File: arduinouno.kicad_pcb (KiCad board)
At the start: 2 copper layers, 0 parts

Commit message: started placement; updated 3d model offsets for PDIP components
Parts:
- added C1: 100u|10V, arduinouno:C_ALUM_C_SIZE, F.Cu at (212.8, 44.3)
- added C10: 18pF, arduinouno:C0805x95mm, F.Cu at (201.9, 71.8)
- added C11: 100nF, arduinouno:C0805x95mm, F.Cu at (214.3, 52.2)
- added C12: 10uF|16V, arduinouno:C0805x145mm, F.Cu at (210.6, 56.0)
- added C13: 10uF|16V, arduinouno:C0805x145mm, F.Cu at (191.9, 75.0)
- added C14: 100nF, arduinouno:C0805x95mm, F.Cu at (195.2, 71.1)
- added C15: 100nF, arduinouno:C0805x95mm, F.Cu at (203.6, 63.6)
- added C16: 100nF, arduinouno:C0805x95mm, F.Cu at (195.2, 69.0)
- added C17: 100nF, arduinouno:C0805x95mm, F.Cu at (191.9, 73.0)
- added C19: 10uF|16V, arduinouno:C0805x145mm, F.Cu at (148.9, 96.2)
- added C2: 100uF|10V, arduinouno:C_ALUM_C_SIZE, F.Cu at (205.4, 55.6)
- added C20: 100nF, arduinouno:C0805x95mm, F.Cu at (147.2, 81.4)
- added C21: 10uF|16V, arduinouno:C0805x145mm, F.Cu at (206.5, 59.5)
- added C22: 10uF|16V, arduinouno:C0805x145mm, F.Cu at (143.4, 96.2)
- added C23: 100nF, arduinouno:C0805x95mm, F.Cu at (143.4, 94.1)
- added C24: 100nF, arduinouno:C0805x95mm, F.Cu at (146.8, 94.1)
- added C25: 18pF, arduinouno:C0805x95mm, F.Cu at (143.8, 79.3)
- added C26: 100nF, arduinouno:C0805x95mm, F.Cu at (200.3, 63.7)
- added C27: 18pF, arduinouno:C0805x95mm, F.Cu at (147.2, 79.3)
- added C28: 100nF, arduinouno:C0805x95mm, F.Cu at (188.5, 76.8)
- added C29: 100nF, arduinouno:C0805x95mm, F.Cu at (210.9, 51.9)
- added C3: 10uF|16V, arduinouno:C0805x145mm, F.Cu at (191.9, 70.9)
- added C30: 100nF, arduinouno:C0805x95mm, F.Cu at (200.3, 61.6)
- added C31: 100nF, arduinouno:C0805x95mm, F.Cu at (210.3, 65.6)
- added C32: 100nF, arduinouno:C0805x95mm, F.Cu at (198.6, 77.2)
- added C33: 100nF, arduinouno:C0805x95mm, F.Cu at (198.4, 67.0)
- added C34: 10uF|16V, arduinouno:C0805x145mm, F.Cu at (198.0, 89.1)
- added C4: 100nF, arduinouno:C0805x95mm, F.Cu at (214.3, 48.1)
- added C5: 100nF, arduinouno:C0805x95mm, F.Cu at (213.7, 60.4)
- added C6: 100nF, arduinouno:C0805x95mm, F.Cu at (201.9, 73.8)
- added C7: 1uF|25V, arduinouno:C0805x95mm, F.Cu at (205.3, 69.7)
- added C8: 100nF, arduinouno:C0805x95mm, F.Cu at (194.6, 79.3)
- added C9: 18pF, arduinouno:C0805x95mm, F.Cu at (205.3, 67.7)
- added D1: GREEN, arduinouno:LED_0603, F.Cu at (197.4, 97.8)
- added D2: ORANGE, arduinouno:LED_0603, F.Cu at (214.8, 84.4)
- added D3: ORANGE, arduinouno:LED_0603, F.Cu at (200.9, 97.8)
- added D4: ORANGE, arduinouno:LED_0603, F.Cu at (197.4, 99.4)
- added D5: BAT54HT1G, arduinouno:SOD323, F.Cu at (194.6, 88.8)
- added D6: BAT54HT1G, arduinouno:SOD323, F.Cu at (181.8, 99.0)
- added FB1: MPZ2012S601AT000, arduinouno:FB0805x85mm, F.Cu at (216.4, 97.7)
- added FB2: MPZ2012S601AT000, arduinouno:FB0805x85mm, F.Cu at (148.9, 98.3)
- added FB3: MPZ2012S601AT000, arduinouno:FB0805x85mm, F.Cu at (146.2, 96.8)
- added FID1: FID_1MM, arduinouno:FID_40x120M, F.Cu at (192.1, 90.1)
- added FID2: FID_1MM, arduinouno:FID_40x120M, F.Cu at (191.1, 90.1)
- added FID3: FID_1MM, arduinouno:FID_40x120M, F.Cu at (181.2, 100.3)
- added FID4: FID_1MM, arduinouno:FID_40x120M, F.Cu at (180.2, 100.3)
- added J1: M20-7820842, arduinouno:8P_Header_Female_2.54mm, F.Cu at (129.5, 101.6)
- added J2: M20-7820646, arduinouno:6P_Header_Female_2.54mm, F.Cu at (152.4, 101.6)
- added J3: M20-7820842, arduinouno:8P_Header_Female_2.54mm, F.Cu at (165.1, 53.3)
- added J4: M20-7821046, arduinouno:10P_Header_Female_2.54mm, F.Cu at (143.3, 53.3)
- added J5: 67997-106HLF, arduinouno:HDR_2x3_2.54mm, F.Cu at (195.4, 51.8)
- added J6: 67997-106HLF, arduinouno:HDR_2x3_2.54mm, F.Cu at (211.5, 94.5)
- added J7: 10118193-0001LF, arduinouno:10118193, F.Cu at (185.3, 93.7)
- added J8: PAD_WITH_HOLE_4mmx1.5mm, arduinouno:PAD_WITH_HOLE_4mmx1.5mm, F.Cu at (208.7, 97.9)
- added J9: PAD_WITH_HOLE_4mmx1.5mm, arduinouno:PAD_WITH_HOLE_4mmx1.5mm, F.Cu at (212.7, 97.9)
- added JP1: 68000-103HLF, arduinouno:3P_Header_2.54mm, F.Cu at (205.3, 92.0)
- added JP2: 68602-104HLF, arduinouno:HDR_2x2_2.54mm, F.Cu at (194.7, 64.6)
- added JP3: 68001-204HLF, arduinouno:4P_Header_2.54mm, F.Cu at (211.6, 81.6)
- added JP4: 68000-103HLF, arduinouno:3P_Header_2.54mm, F.Cu at (192.7, 49.2)
- added L1: 2u2|2A, arduinouno:C1210_INDUCTOR, F.Cu at (215.9, 81.9)
- added MH1: MH_7.4MMCx3.2MMD, arduinouno:MH_7.4MMCx3.2MMD, F.Cu at (115.6, 101.6)
- added MH2: MH_7.4MMCx3.2MMD, arduinouno:MH_7.4MMCx3.2MMD, F.Cu at (167.6, 96.5)
- added MH3: MH_7.4MMCx3.2MMD, arduinouno:MH_7.4MMCx3.2MMD, F.Cu at (167.6, 68.6)
- added MH4: MH_7.4MMNCx3.2MMD, arduinouno:MH_7.4MMCx3.2MMD_NON_COPPER_NPTH, F.Cu at (116.8, 53.3)
- added R1: 100K, arduinouno:R0805x60mm, F.Cu at (217.6, 48.3)
- added R10: 1k, arduinouno:R0805x60mm, F.Cu at (207.0, 61.5)
- added R11: 1k, arduinouno:R0805x60mm, F.Cu at (207.0, 63.6)
- added R12: 1k, arduinouno:R0805x60mm, F.Cu at (195.2, 75.2)
- added R13: 22R, arduinouno:R0805x60mm, F.Cu at (139.9, 94.1)
- added R14: 10k, arduinouno:R0805x60mm, F.Cu at (162.7, 81.4)
- added R15: 560R, arduinouno:R0805x60mm, F.Cu at (198.6, 71.1)
- added R16: 1M, arduinouno:R0805x60mm, F.Cu at (143.8, 81.4)
- added R17: 560R, arduinouno:R0805x60mm, F.Cu at (201.9, 67.7)
- added R18: 10k, arduinouno:R0805x60mm, F.Cu at (213.2, 58.4)
- added R19: 10k, arduinouno:R0805x60mm, F.Cu at (201.9, 69.7)
- added R2: 560R, arduinouno:R0805x60mm, F.Cu at (187.9, 79.8)
- added R20: 10k, arduinouno:R0805x60mm, F.Cu at (191.3, 81.2)
- added R21: 10k, arduinouno:R0805x60mm, F.Cu at (198.6, 73.1)
- added R22: 560R, arduinouno:R0805x60mm, F.Cu at (217.3, 54.5)
- added R23: 22R, arduinouno:R0805x60mm, F.Cu at (195.2, 77.2)
- added R24: 22R, arduinouno:R0805x60mm, F.Cu at (207.0, 65.6)
- added R25: 22R, arduinouno:R0805x60mm, F.Cu at (210.3, 61.5)
- added R26: 0R, arduinouno:R0805x60mm, F.Cu at (210.3, 63.6)
- added R27: 0R, arduinouno:R0805x60mm, F.Cu at (217.3, 56.5)
- added R28: 0R, arduinouno:R0805x60mm, F.Cu at (198.6, 75.2)
- added R3: 560R, arduinouno:R0805x60mm, F.Cu at (198.6, 69.0)
- added R4: 10k, arduinouno:R0805x60mm, F.Cu at (217.6, 50.4)
- added R5: 22R, arduinouno:R0805x60mm, F.Cu at (209.9, 59.5)
- added R6: 22R, arduinouno:R0805x60mm, F.Cu at (214.0, 54.3)
- added R7: 22R, arduinouno:R0805x60mm, F.Cu at (191.9, 77.1)
- added R8: 0R, arduinouno:R0805x60mm, F.Cu at (195.2, 73.1)
- added R9: 1M, arduinouno:R0805x60mm, F.Cu at (203.6, 65.6)
- added SCKT_FOR_U1: 28-DIP Socket, arduinouno:28DIP_7.62MM_SCKT, F.Cu at (163.7, 83.9)
- added SW1: 1825910-6, arduinouno:1825910-6, F.Cu at (195.5, 44.7)
- added SW2: 1825910-6, arduinouno:1825910-6, F.Cu at (199.7, 93.9)
- added U1: ATMEGA328P-PU, arduinouno:28PIN_PDIP_7.62mm, F.Cu at (163.7, 83.9)
- added U2: ATMEGA16U2-AU, arduinouno:QFP-32_8.4x8.4_Pitch0.8mm, F.Cu at (117.0, 74.1)
- added U3: TL1963A-33DCQR, arduinouno:DCQ_R-PDSO-G6, F.Cu at (183.2, 105.0)
- added U4: SN74AHC1G09DBVR, arduinouno:DBV_SOT23_5, F.Cu at (188.5, 71.8)
- added U5: SN74AHC1G09DBVR, arduinouno:DBV_SOT23_5, F.Cu at (210.9, 49.0)
- added U6: SN74AHC1G09DBVR, arduinouno:DBV_SOT23_5, F.Cu at (218.0, 43.4)
- added U7: SN74AHC1G09DBVR, arduinouno:DBV_SOT23_5, F.Cu at (208.4, 92.6)
- added Y1: 16.000MHz, arduinouno:ABM7_BIG, F.Cu at (145.4, 76.2)
- added Y2: 16.000MHz, arduinouno:ABM7_BIG, F.Cu at (217.0, 87.3)
- added Z1: CG0603MLC-05E, arduinouno:R_0603, F.Cu at (200.4, 99.4)
- added Z2: CG0603MLC-05E, arduinouno:R_0603, F.Cu at (203.3, 99.4)
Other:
- board outline added: 68.6 x 53.3 mm

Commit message: finished placement
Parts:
- moved C1 114.4 mm to (108.8, 92.0), turned to 90 degrees
- moved L1 113.1 mm to (103.7, 96.3), turned to 270 degrees
- moved J6 111.2 mm to (104.1, 65.5)
- moved R4 110.1 mm to (110.8, 76.8), turned to 90 degrees
- moved J9 109.1 mm to (103.8, 90.8)
- moved U5 107.2 mm to (107.7, 77.9)
- moved R6 107.1 mm to (110.8, 82.9)
- moved C2 106.4 mm to (108.8, 100.1), turned to 90 degrees
- moved J8 105.0 mm to (103.8, 101.8)
- moved C12 103.9 mm to (113.1, 91.9), turned to 90 degrees
- moved C31 100.7 mm to (110.8, 81.0)
- moved R1 100.2 mm to (118.7, 64.3), turned to 270 degrees
- moved R5 99.9 mm to (110.4, 69.1), turned to 180 degrees
- moved C4 98.8 mm to (121.2, 81.1), turned to 270 degrees
- moved R26 98.1 mm to (114.2, 82.9), turned to 180 degrees
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
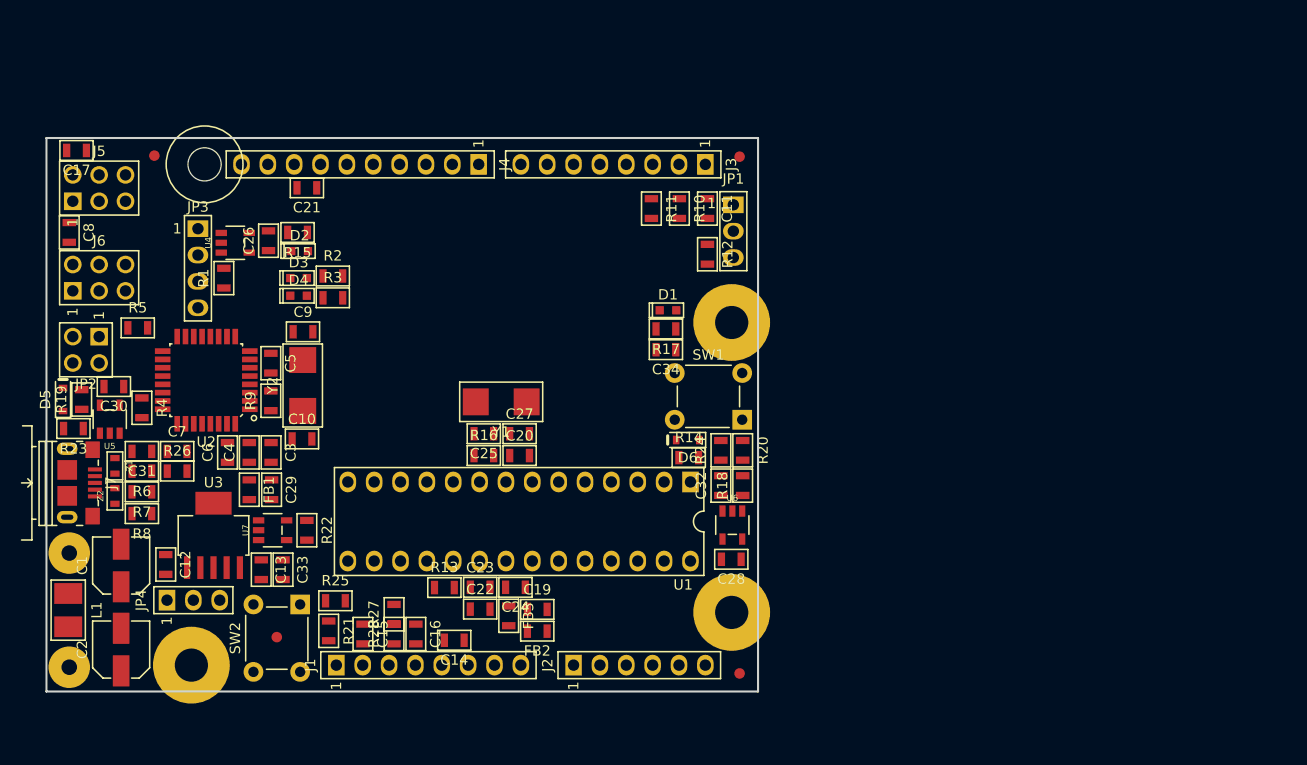
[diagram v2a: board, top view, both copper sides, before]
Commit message: updated design rules and net classes
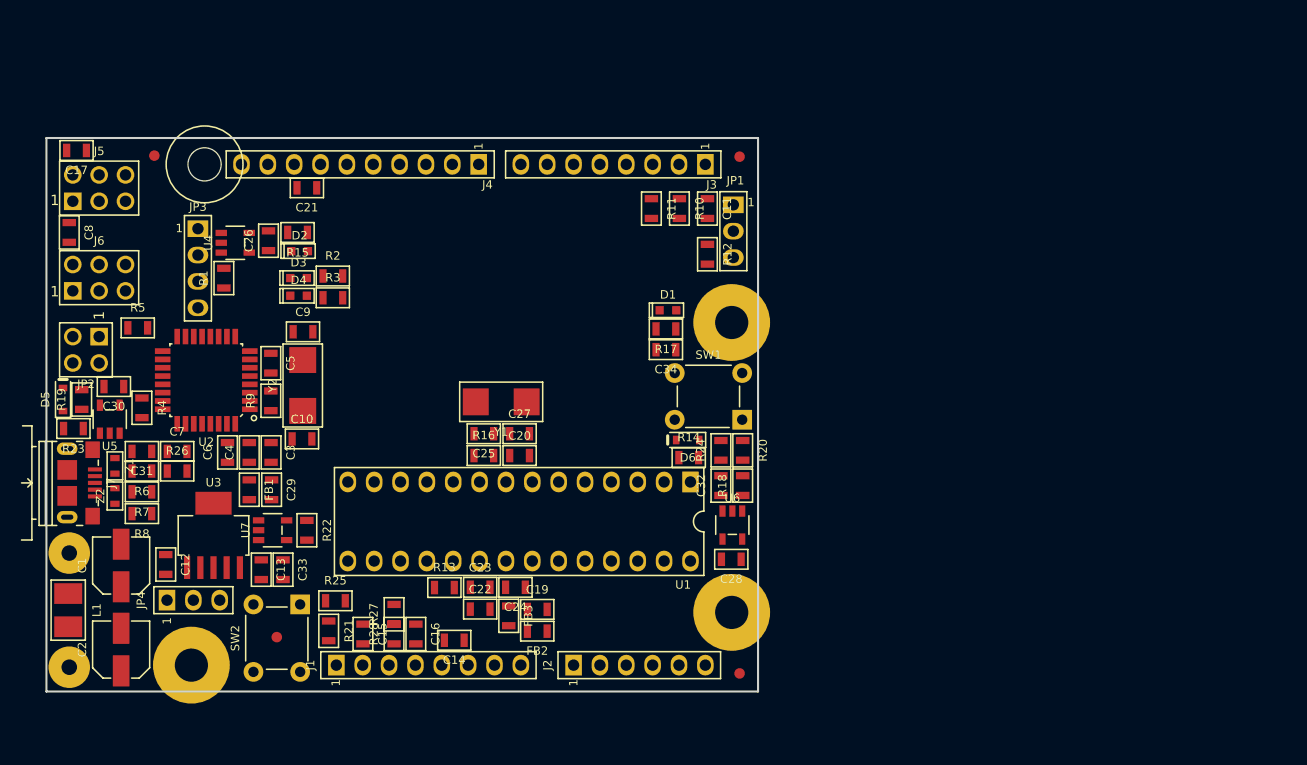
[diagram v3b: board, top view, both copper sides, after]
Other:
- net class Default: clearance 0.2 -> 0.2032; trace_width 0.25 -> 0.2032; via_dia 0.8 -> 0.6048; via_drill 0.4 -> 0.3
- net class Power added: clearance 0.2032, trace_width 0.4, via_dia 0.6048, via_drill 0.3
- rule trace_clearance: 0.2 -> 0.2032
- rule trace_min: 0.2 -> 0.1524
- rule via_min_size: 0.4 -> 0.6048

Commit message: layout continuing
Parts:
- moved R3 4.22 mm to (129.6, 62.0)
- moved R2 4.22 mm to (129.6, 59.9)
- moved C25 3.45 mm to (147.2, 79.3), turned to 180 degrees
- moved C27 3.40 mm to (143.8, 79.3), turned to 0 degrees
- moved U3 0.56 mm to (117.8, 89.7)
- moved C10 0.40 mm to (126.6, 79.8)
- moved C5 0.40 mm to (123.6, 72.5)
- moved R9 0.40 mm to (123.6, 76.1)
- moved Y2 0.40 mm to (126.7, 74.7)
- moved C7 0.40 mm to (114.6, 81.0)
- moved C9 0.40 mm to (126.7, 69.5)
- moved R26 0.40 mm to (114.6, 82.9)
- moved C3 0.35 mm to (123.6, 81.1)
- moved C29 0.30 mm to (123.6, 84.7)
- moved FB1 0.30 mm to (121.5, 84.7)
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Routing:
- net /328P_RESETn: track 0.00 -> 133.9 mm, vias 0 -> 1
- net /AD5_SCL: track 0.00 -> 95.4 mm
- net +AREF: track 0.00 -> 92.7 mm, vias 0 -> 2
- net /AD4_SDA: track 0.00 -> 89.4 mm
- net +5V: track 0.00 -> 85.9 mm
- net /SCK: track 0.00 -> 85.2 mm
- net /MISO: track 0.00 -> 84.6 mm, vias 0 -> 1
- net /MOSI: track 0.00 -> 81.0 mm
- net /16U2PROG_328P_RESETn: track 0.00 -> 58.7 mm, vias 0 -> 2
- net /16U2_TXD: track 0.00 -> 50.6 mm, vias 0 -> 2
- net /16U2_RXD: track 0.00 -> 48.2 mm, vias 0 -> 2
- net /IO9: track 0.00 -> 42.9 mm, vias 0 -> 2
- net /IO8: track 0.00 -> 42.4 mm, vias 0 -> 1
- net /SS: track 0.00 -> 41.4 mm, vias 0 -> 2
- net /IO7: track 0.00 -> 36.5 mm
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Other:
- net class Default: trace_width 0.2032 -> 0.3

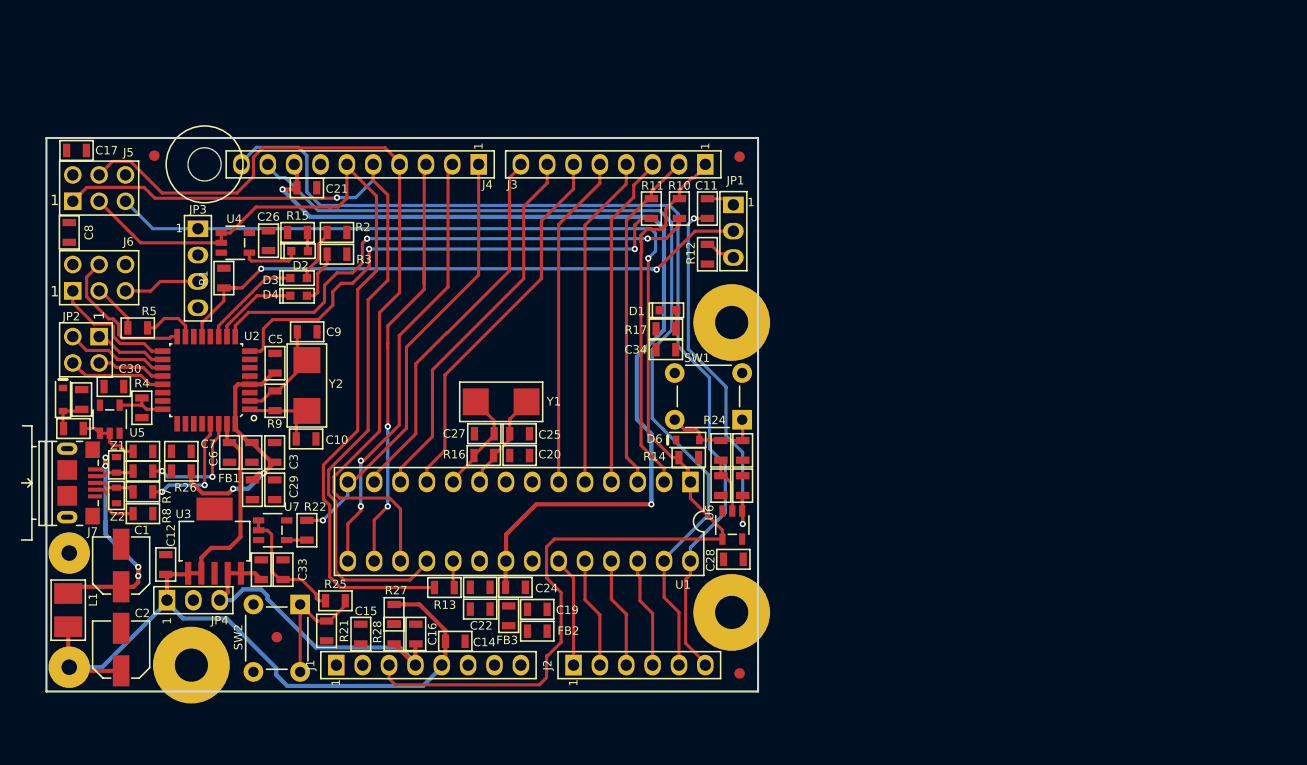
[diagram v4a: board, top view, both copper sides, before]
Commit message: routed power nets 5V, 3V3, 5/3V3
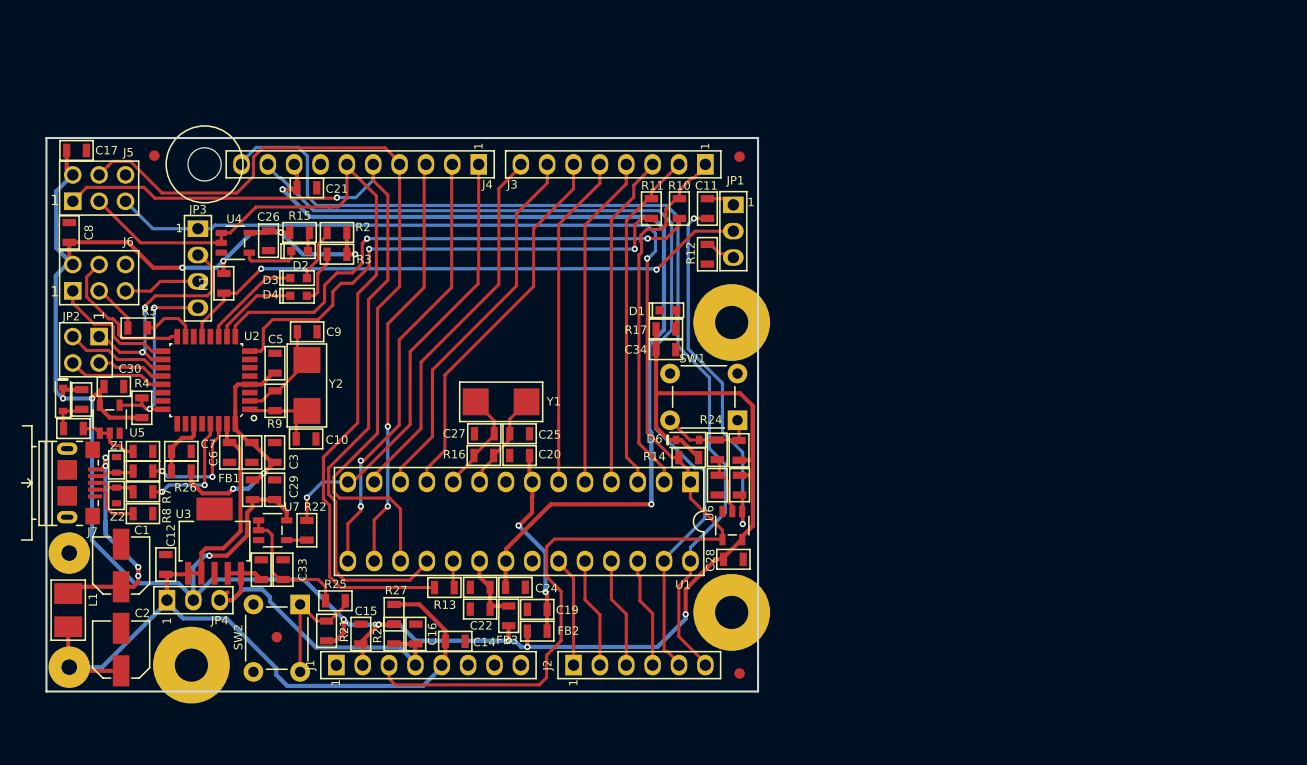
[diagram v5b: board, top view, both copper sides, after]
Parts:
- moved R1 0.50 mm to (118.7, 64.8)
- moved SW1 0.45 mm to (164.9, 75.8)
- moved R24 0.35 mm to (166.2, 80.8)
- moved C32 0.35 mm to (166.2, 84.2)
- moved R20 0.35 mm to (168.3, 80.9)
- moved R18 0.30 mm to (168.4, 84.2)
- moved R15 0.20 mm to (126.0, 59.9)
- moved U6 0.05 mm to (167.7, 88.2)
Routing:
- net +5V_3V3: track 0.00 -> 246.6 mm, vias 0 -> 12
- net /+5_3V3_328P_VCC: track 0.00 -> 18.8 mm, vias 0 -> 2
- net /16U2_PB4: track 7.03 -> 22.8 mm, vias 0 -> 2
- net /16U2_RESETn: track 5.00 -> 19.1 mm, vias 0 -> 2
- net /+5_3V3_328P_AVCC: track 0.00 -> 6.97 mm
- net /+3V3_16U2_UCAP: track 0.00 -> 6.00 mm
- net /16U2PROG_328P_RESETn: track 58.7 -> 56.7 mm
- net +AREF: track 92.7 -> 90.9 mm
- net +3V3: track 34.0 -> 35.6 mm
- net /SS: track 41.4 -> 40.2 mm
- net /328P_RESETn: track 133.9 -> 134.8 mm
- net /USER_BUTTON_BUF: track 12.5 -> 13.1 mm
- net /AD5_SCL: track 95.4 -> 95.9 mm
- net /IO8: track 42.4 -> 42.9 mm

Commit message: updated ground vias
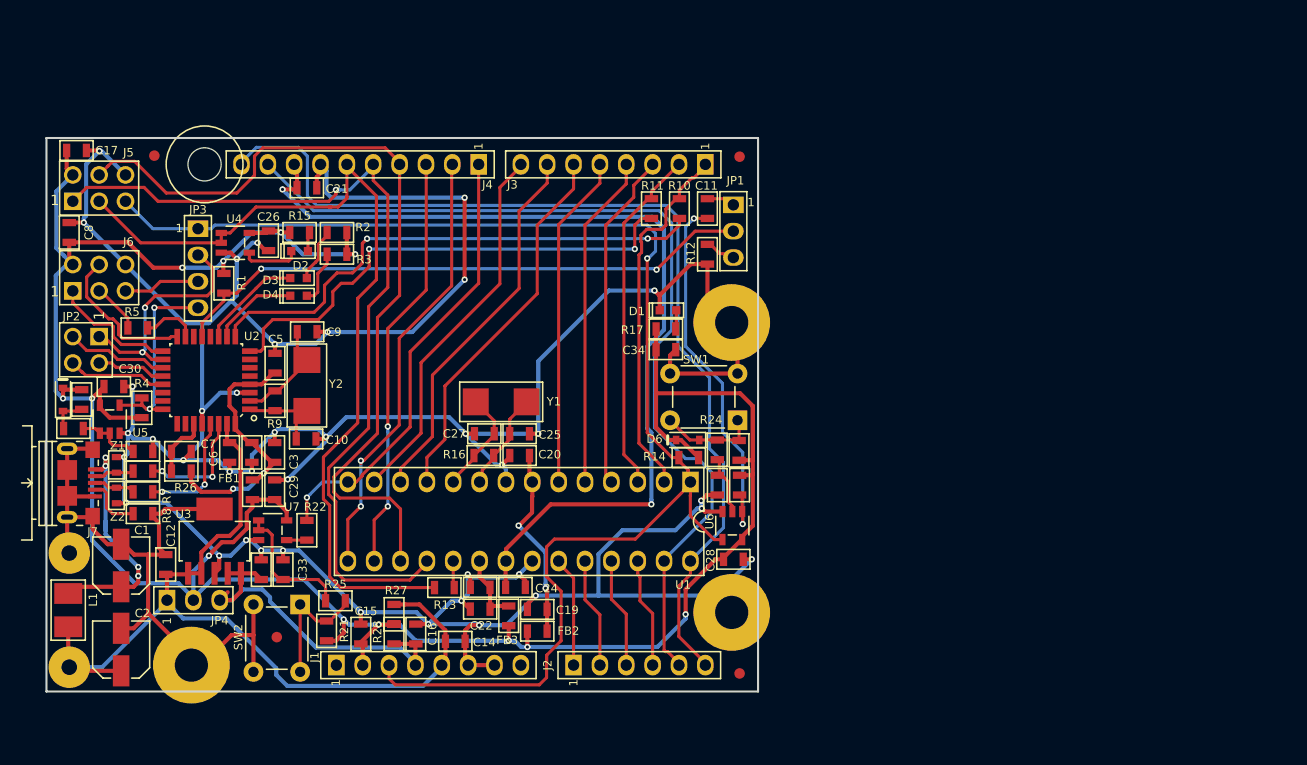
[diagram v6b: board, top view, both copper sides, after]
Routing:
- net GND: track 0.00 -> 447.0 mm, vias 0 -> 39
- net /AD4_SDA: track 89.3 -> 90.1 mm
- net +5V_3V3: track 246.6 -> 246.0 mm
- net /+5_3V3_16U2: track 26.0 -> 26.6 mm

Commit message: power polys done, before ground poly
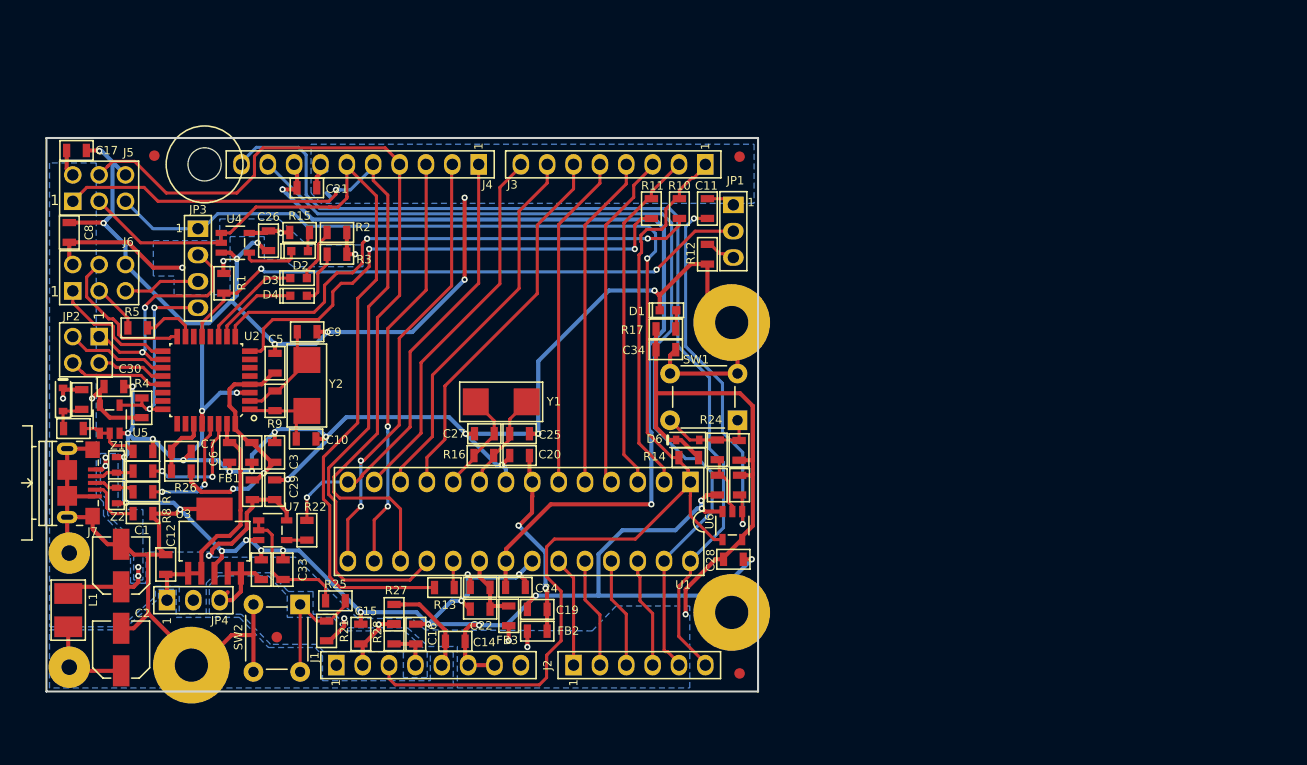
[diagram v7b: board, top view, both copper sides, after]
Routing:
- net +5V_3V3: track 246.0 -> 117.5 mm
- net +5V: track 85.5 -> 42.2 mm
- net +3V3: track 35.6 -> 12.9 mm
- net GND: track 447.0 -> 432.0 mm, vias 39 -> 40
- net /+5V_USB: track 24.7 -> 10.6 mm
- net +AREF: track 91.1 -> 89.1 mm
- net /328P_RESETn: track 134.7 -> 135.6 mm
- added copper zone on B.Cu, net +3V3
- added copper zone on B.Cu, net +5V
- added copper zone on B.Cu, net +5V_3V3
- added copper zone on B.Cu, net /+5V_USB
- added copper zone on B.Cu, net GND

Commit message: after ground poly
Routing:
- net GND: track 432.0 -> 165.6 mm, vias 40 -> 39
